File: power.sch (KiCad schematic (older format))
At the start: 65 parts, among them U1 SAMA5D2x-SIP

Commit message: Connected Unit F
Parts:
- added R?: 0R, Resistor_SMD:R_0603_1608Metric, symbol Device:R_Small
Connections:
- net labels added: VDDA
- wire segments 249 -> 254
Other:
- note added: "Plane fill for \nall USB components"
- moved on the sheet: C13, C29, C30, C31, C32, C33, C34, C35, C36, C37, C38, C39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

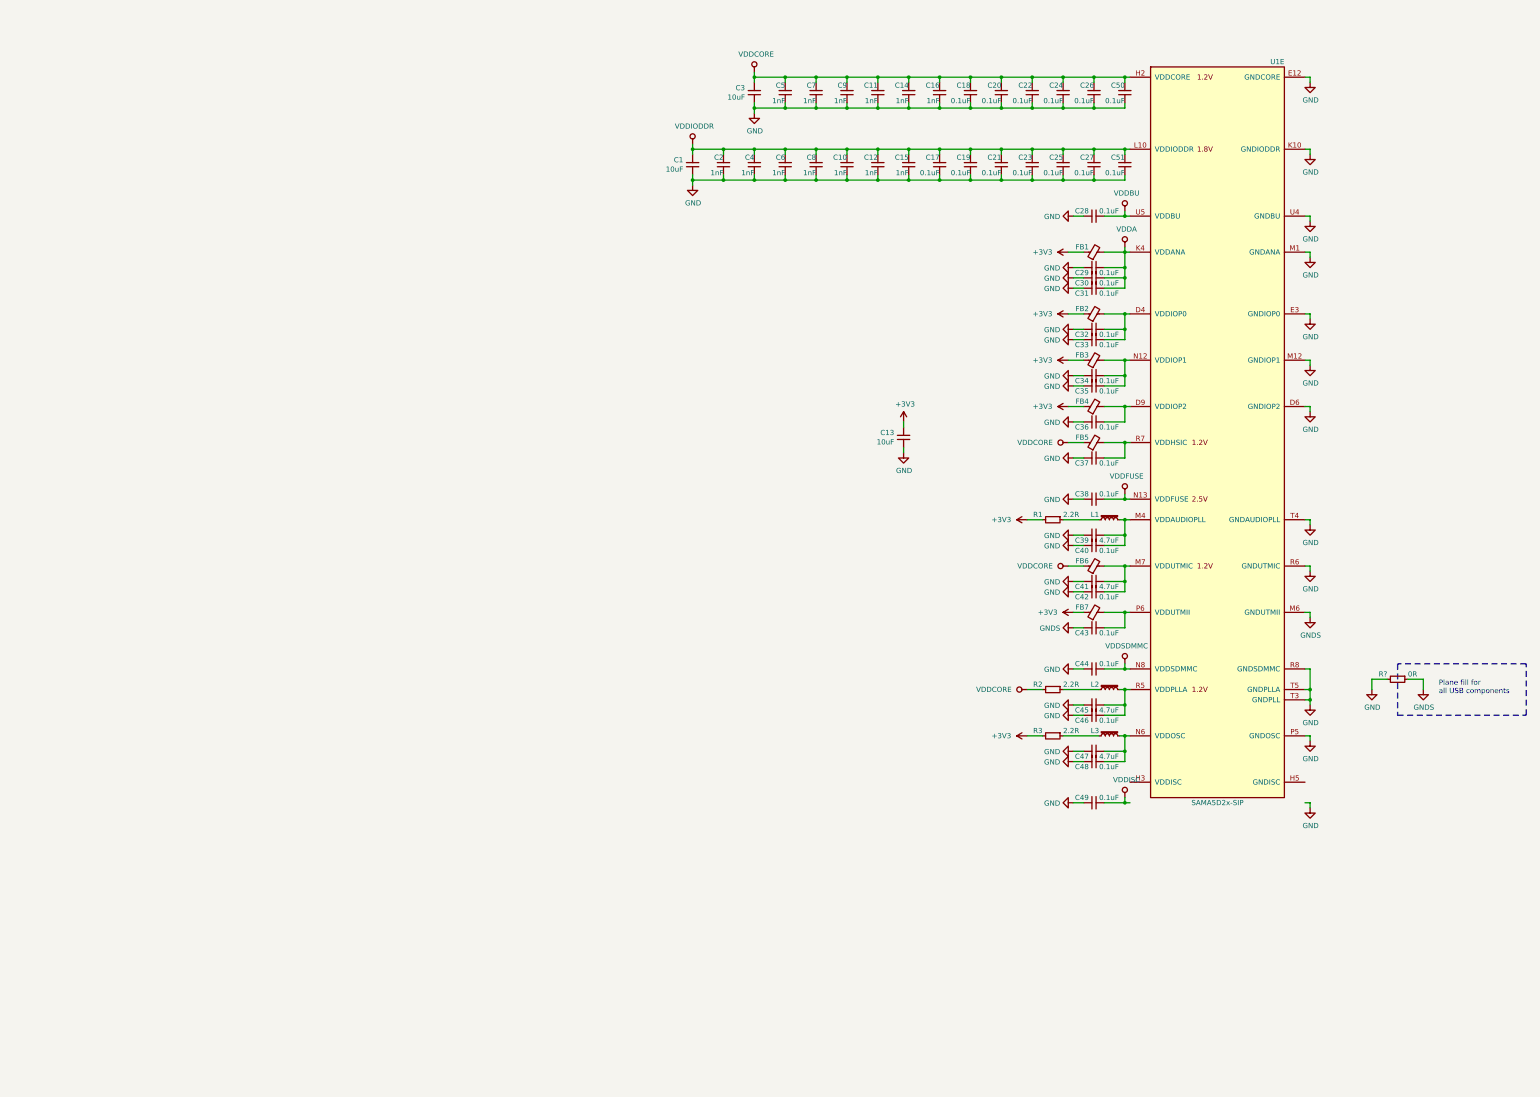
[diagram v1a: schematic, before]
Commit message: Added QSPI Flash and started work on PMIC
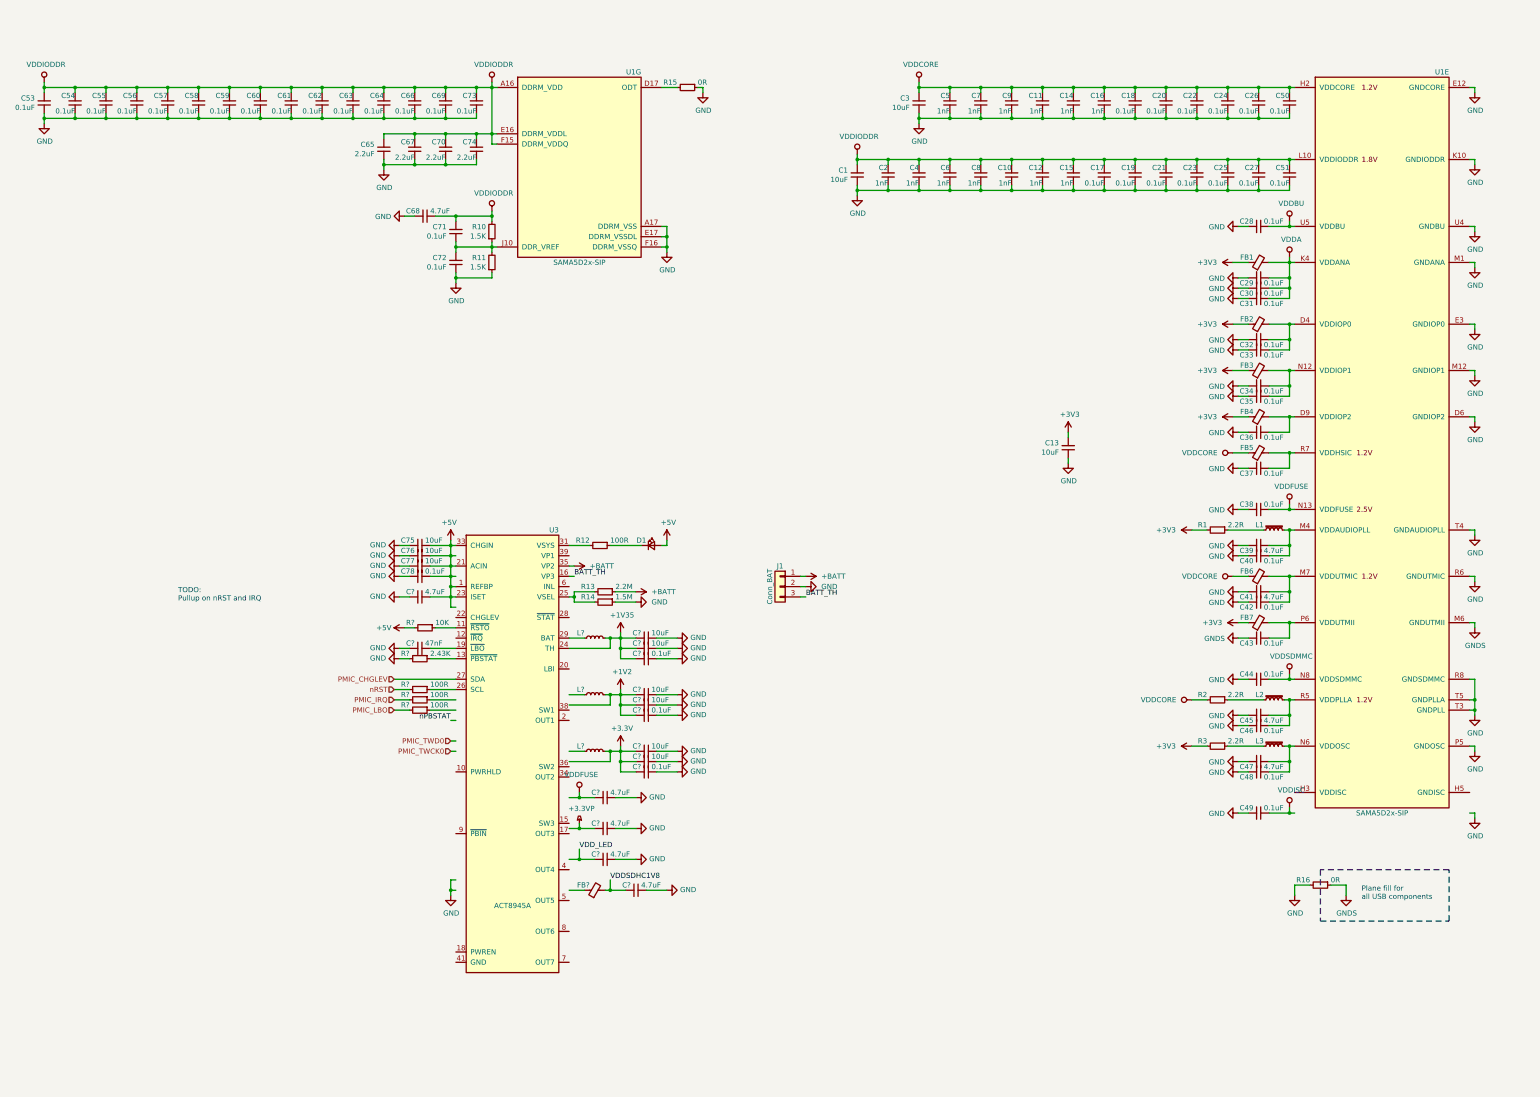
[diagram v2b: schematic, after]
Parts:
- added C53, C54, C55, C56, C57, C58, C59, C60, C61, C62, C63, C64, C66, C69, C73, C78, C? (x3): 0.1uF, Capacitor_SMD:C_0603_1608Metric, symbol Device:C_Small
- added C65, C67, C70, C74: 2.2uF, Capacitor_SMD:C_0603_1608Metric, symbol Device:C_Small
- added C68, C? (x5): 4.7uF, Capacitor_SMD:C_0603_1608Metric, symbol Device:C_Small
- added C71, C72: 0.1uF, symbol Device:C_Small
- added C75, C76, C77, C? (x6): 10uF, Capacitor_SMD:C_0603_1608Metric, symbol Device:C_Small
- added C?: 47nF, Capacitor_SMD:C_0603_1608Metric, symbol Device:C_Small
- added D1: LED_CHARGE, symbol Device:LED_Small
- added FB?: BLM18PG181SN1D, Inductor_SMD:L_0603_1608Metric, symbol Device:Ferrite_Bead_Small
- added J1: Conn_BAT, symbol Connector_Generic:Conn_01x03
- added L? (x3): LQM2HPN2R2MG0L, symbol Device:L_Small
- added R10, R11: 1.5K, symbol Device:R_Small
- added R12, R? (x3): 100R, symbol Device:R_Small
- added R13: 2.2M, symbol Device:R_Small
- added R14: 1.5M, symbol Device:R_Small
- added R15: 0R, symbol Device:R_Small
- added R?: 10K, symbol Device:R_Small
- added R?: 2.43K, symbol Device:R_Small
- added unit 7 of U1
- added U3: ACT8945A, symbol Power_Management_Extra:ACT8945A
- gave numbers to parts that had none: 1
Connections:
- net labels added: +1V2, +1V35, +3.3V, +3.3VP, +5V, +BATT, BATT_TH, PMIC_CHGLEV, PMIC_IRQ, PMIC_LBO, PMIC_TWCK0, PMIC_TWD0, VDDSDHC1V8, VDD_LED, nPBSTAT, nRST
- wire segments 254 -> 481
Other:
- note added: "TODO:\nPullup on nRST and IRQ\n"
- moved on the sheet: C1, C10, C11, C12, C13, C14, C15, C16, C17, C18, C19, C2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

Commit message: Finished power, added microSD, USB A, btn
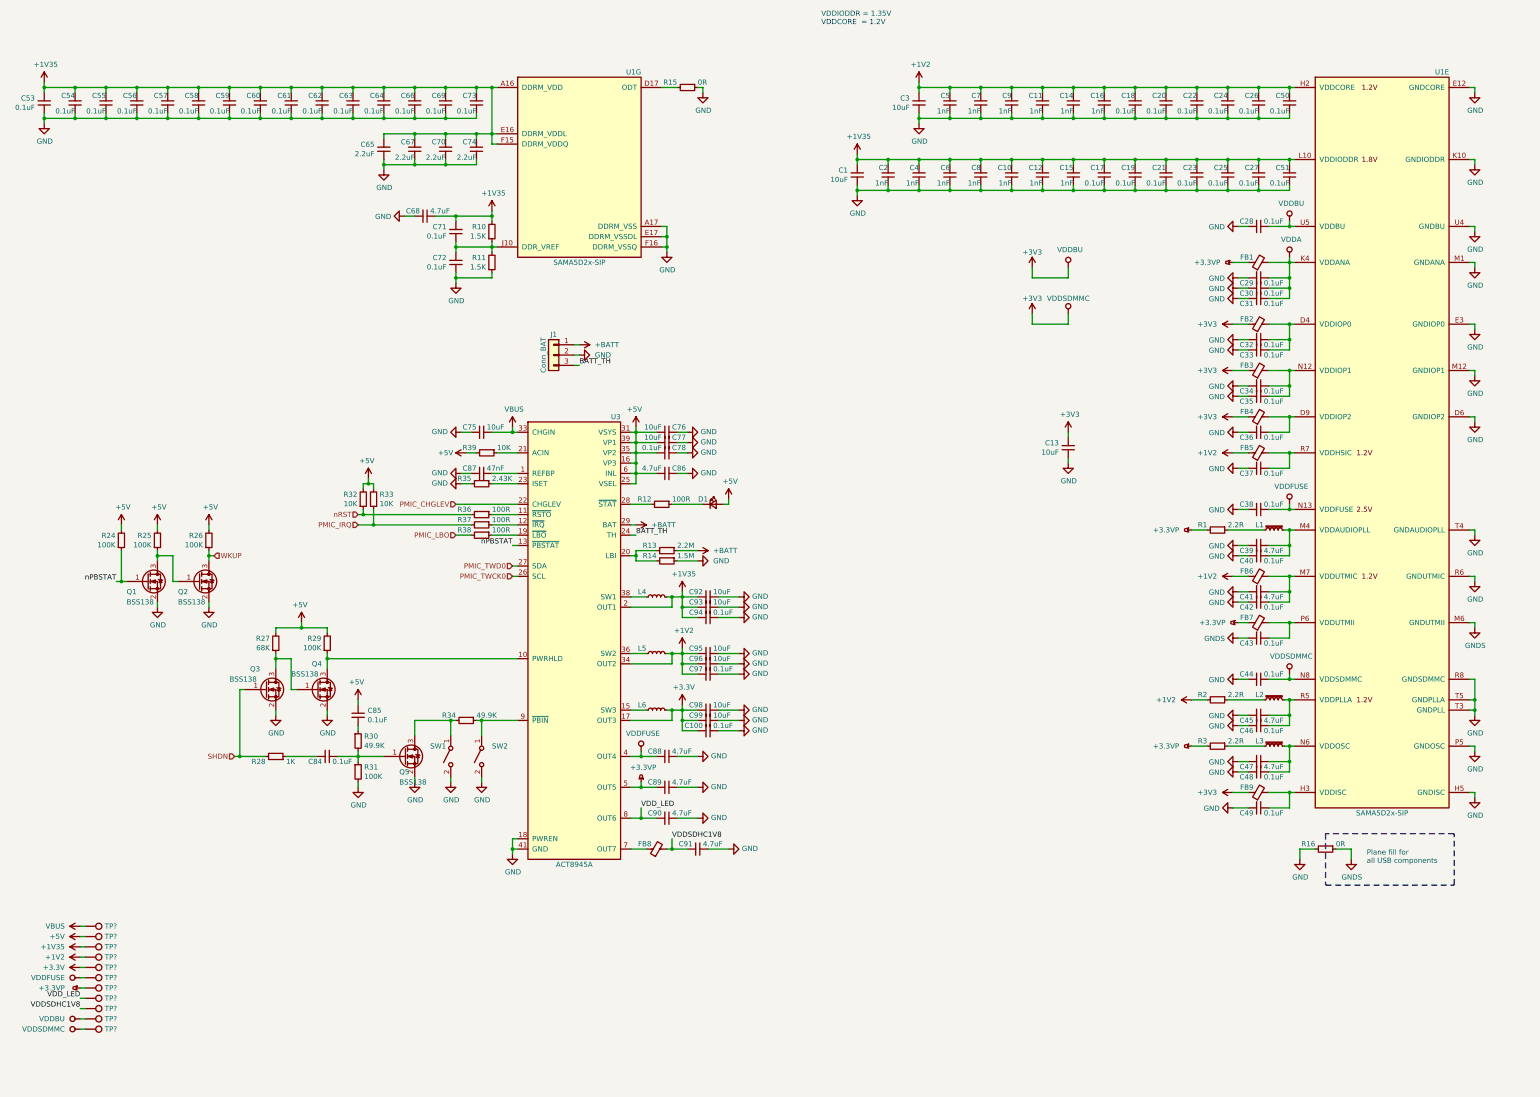
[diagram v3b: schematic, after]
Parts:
- added C84: 0.1uF, Capacitor_SMD:C_0603_1608Metric, symbol Device:C_Small
- added C85: 0.1uF, symbol Device:C_Small
- added FB9: BLM03AX100SZ1, Inductor_SMD:L_0603_1608Metric, symbol Device:Ferrite_Bead_Small
- added Q1, Q2, Q3, Q4, Q5: BSS138, Package_TO_SOT_SMD:SOT-23, symbol Transistor_FET:BSS138
- added R24, R25, R26, R29, R31: 100K, symbol Device:R_Small
- added R27: 68K, symbol Device:R_Small
- added R28: 1K, symbol Device:R_Small
- added R30, R34: 49.9K, symbol Device:R_Small
- added R32, R33: 10K, symbol Device:R_Small
- added SW1: SW_WAKEUP, symbol Switch:SW_SPST
- added SW2: SW_RESET, symbol Switch:SW_SPST
- added TP?: TP_VBUS, symbol Connector:TestPoint
- added TP?: TP_5V, symbol Connector:TestPoint
- added TP?: TP_1.35V, symbol Connector:TestPoint
- added TP?: TP_1.2V, symbol Connector:TestPoint
- added TP?: TP_3.3V, symbol Connector:TestPoint
- added TP?: TP_VDDFUSE, symbol Connector:TestPoint
- added TP?: TP_3.3VP, symbol Connector:TestPoint
- added TP?: TP_VDD_LED, symbol Connector:TestPoint
- added TP?: TP_VDDSDHC1V8, symbol Connector:TestPoint
- added TP?: TP_VDDBU, symbol Connector:TestPoint
- added TP?: TP_VDDSDMMC, symbol Connector:TestPoint
- gave numbers to parts that had none: 24
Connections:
- net labels added: SHDN, VBUS, WKUP
- net labels removed: VDDCORE, VDDIODDR, VDDISC
- wire segments 481 -> 561
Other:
- note added: "VDDIODDR = 1.35V\nVDDCORE = 1.2V"
- note removed: "TODO:\nPullup on nRST and IRQ\n"
- moved on the sheet: C100, C49, C75, C76, C77, C78, C86, C87, C88, C89, C90, C91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
